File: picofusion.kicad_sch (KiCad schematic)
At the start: 33 parts, among them J1 NORTH, J2 EAST, J3 WEST, J4 SOUTH, U1 W25Q16, U2 RP2040, Y1 12MHz

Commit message: draft: schematic and layout for H20R1
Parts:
- removed C13, C15, C24, C26: 0.1uF, Capacitor_SMD:C_0201_0603Metric, symbol Device:C
- removed C25: 1uF, Capacitor_SMD:C_0201_0603Metric, symbol Device:C
- removed R2, R3: 27, Resistor_SMD:R_0201_0603Metric, symbol Device:R
- removed R4, R5: 10K, Resistor_SMD:R_0402_1005Metric, symbol Device:R
- removed U1: W25Q16, USON:8-USON, symbol Memory_Flash:W25Q32JVSS
- removed U2: RP2040, RP2040_minimal:RP2040-QFN-56, symbol MCU_RaspberryPi_RP2040:RP2040
- added U1: STM32F412CGUx, Package_DFN_QFN:QFN-48-1EP_7x7mm_P0.5mm_EP5.6x5.6mm, symbol MCU_ST_STM32F4:STM32F412CGUx
- C1: value 0.1uF -> 2u2
- C10: value 0.1uF -> 1u0
- C2, C4, C7, C9: value 0.1uF -> 0u1
- C3: value 1uF -> 0u1
- C6: value 0.1uF -> 4u7
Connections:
- net +3V3: now also C2.1, C3.1, U1.1 (VBAT), U1.24 (VDD), U1.36 (VDD), U1.48 (VDD), U1.9 (VDDA)
- net 3V3_SENSE: now also U1.15 (PA5)
- net 5V_SENSE: now also U1.14 (PA4)
- net BOOTSEL: now also U1.44 (BOOT0)
- net BUZZER: now also U1.18 (PB0)
- net CAN_SILENT: now also U1.3 (PC14)
- net DRDY_ICM42605: now also U1.30 (PA9)
- net GND: now also C1.1, U1.23 (VSS), U1.35 (VSS), U1.47 (VSS), U1.49 (VSS), U1.8 (VSSA); no longer C1.2
- net IMU_HEATER: now also U1.4 (PC15)
- net NEOPIXEL_3V3: now also U1.39 (PB3)
- net RESV1: now also U1.19 (PB1)
- net SPI0_PICO: now also U1.28 (PB15)
- net SPI0_POCI: now also U1.27 (PB14)
- net SPI0_SCK: now also U1.26 (PB13)
- net SPI0_nCS: now also U1.25 (PB12)
- net SWCLK: now also U1.37 (PA14)
- net SWDIO: now also U1.34 (PA13)
- net UART1_RX_GNSS: now also U1.38 (PA15)
- net UART1_TX_GNSS: now also U1.31 (PA10)
- net USB_DN: now also U1.32 (PA11)
- net USB_DP: now also U1.33 (PA12)
- net XIN: now also U1.5 (PH0)
- net XOUT: now also U1.6 (PH1)
- removed net +1V1: C1.1, C2.1, C3.1
- net I2C0_SCL renamed I2C1_SCL
- net I2C1_SCL: now also U1.42 (PB6)
- net I2C0_SDA renamed I2C1_SDA
- net I2C1_SDA: now also U1.43 (PB7)
- net RUN renamed nRST
- net nRST: now also U1.7 (NRST)
- net SD_nCD renamed SDIO_D0
- net SDIO_D0: now also U1.40 (PB4)
- net SPI1_PICO_SD renamed SDIO_D2
- net SDIO_D2: now also U1.17 (PA7)
- net SPI1_POCI_SD renamed SDIO_D3
- net SDIO_D3: now also U1.41 (PB5)
- net SPI1_SCK_SD renamed SDIO_CMD
- net SDIO_CMD: now also U1.16 (PA6)
- net SPI1_nCS_SD renamed SDIO_D1
- net SDIO_D1: now also U1.29 (PA8)
- net UART0_CTS_TELEM renamed UART2_CTS_TELEM
- net UART2_CTS_TELEM: now also U1.10 (PA0)
- net UART0_RTS_TELEM renamed UART2_RTS_TELEM
- net UART2_RTS_TELEM: now also U1.11 (PA1)
- net UART0_RX_TELEM renamed UART2_RX_TELEM
- net UART2_RX_TELEM: now also U1.13 (PA3)
- net UART0_TX_TELEM renamed UART2_TX_TELEM
- net UART2_TX_TELEM: now also U1.12 (PA2)
- new net: C1.2, U1.22 (VCAP_1)
- new net CAN1_RX: U1.45 (PB8)
- new net CAN1_TX: U1.46 (PB9)
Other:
- note added: "8MHz Crystal"
- note removed: "12MHz Crystal"
- note removed: "Flash"

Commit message: h20r1: more updates
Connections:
- net CAN_SILENT: now also U1.2 (PC13); no longer U1.3 (PC14)
- net IMU_HEATER: now also U1.3 (PC14); no longer U1.4 (PC15)
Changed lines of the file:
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@@
   (no_connect (at 265.43 24.13))
   (no_connect (at 69.85 88.9))
-  (no_connect (at 69.85 73.66))
+  (no_connect (at 69.85 78.74))
   (no_connect (at 265.43 21.59))
   (wire (pts (xy 54.61 60.96) (xy 49.53 60.96))
@@
     (stroke (width 0) (type default) (color 0 0 0 0))
   )
-  (wire (pts (xy 52.07 78.74) (xy 69.85 78.74))
+  (wire (pts (xy 52.07 73.66) (xy 69.85 73.66))
     (stroke (width 0) (type default) (color 0 0 0 0))
   )
@@
     (effects (font (size 1.27 1.27)) (justify left bottom))
   )
-  (label "IMU_HEATER" (at 52.07 78.74 0)
+  (label "IMU_HEATER" (at 52.07 76.2 0)
     (effects (font (size 1.27 1.27)) (justify left bottom))
   )
@@
     (effects (font (size 1.27 1.27)) (justify left bottom))
   )
-  (label "CAN_SILENT" (at 52.07 76.2 0)
-    (effects (font (size 1.27 1.27)) (justify left bottom))
-  )
+  (label "CAN_SILENT" (at 52.07 73.66 0)
+    (effects (font (size 1.27 1.27)) (justify left bottom))
+  )

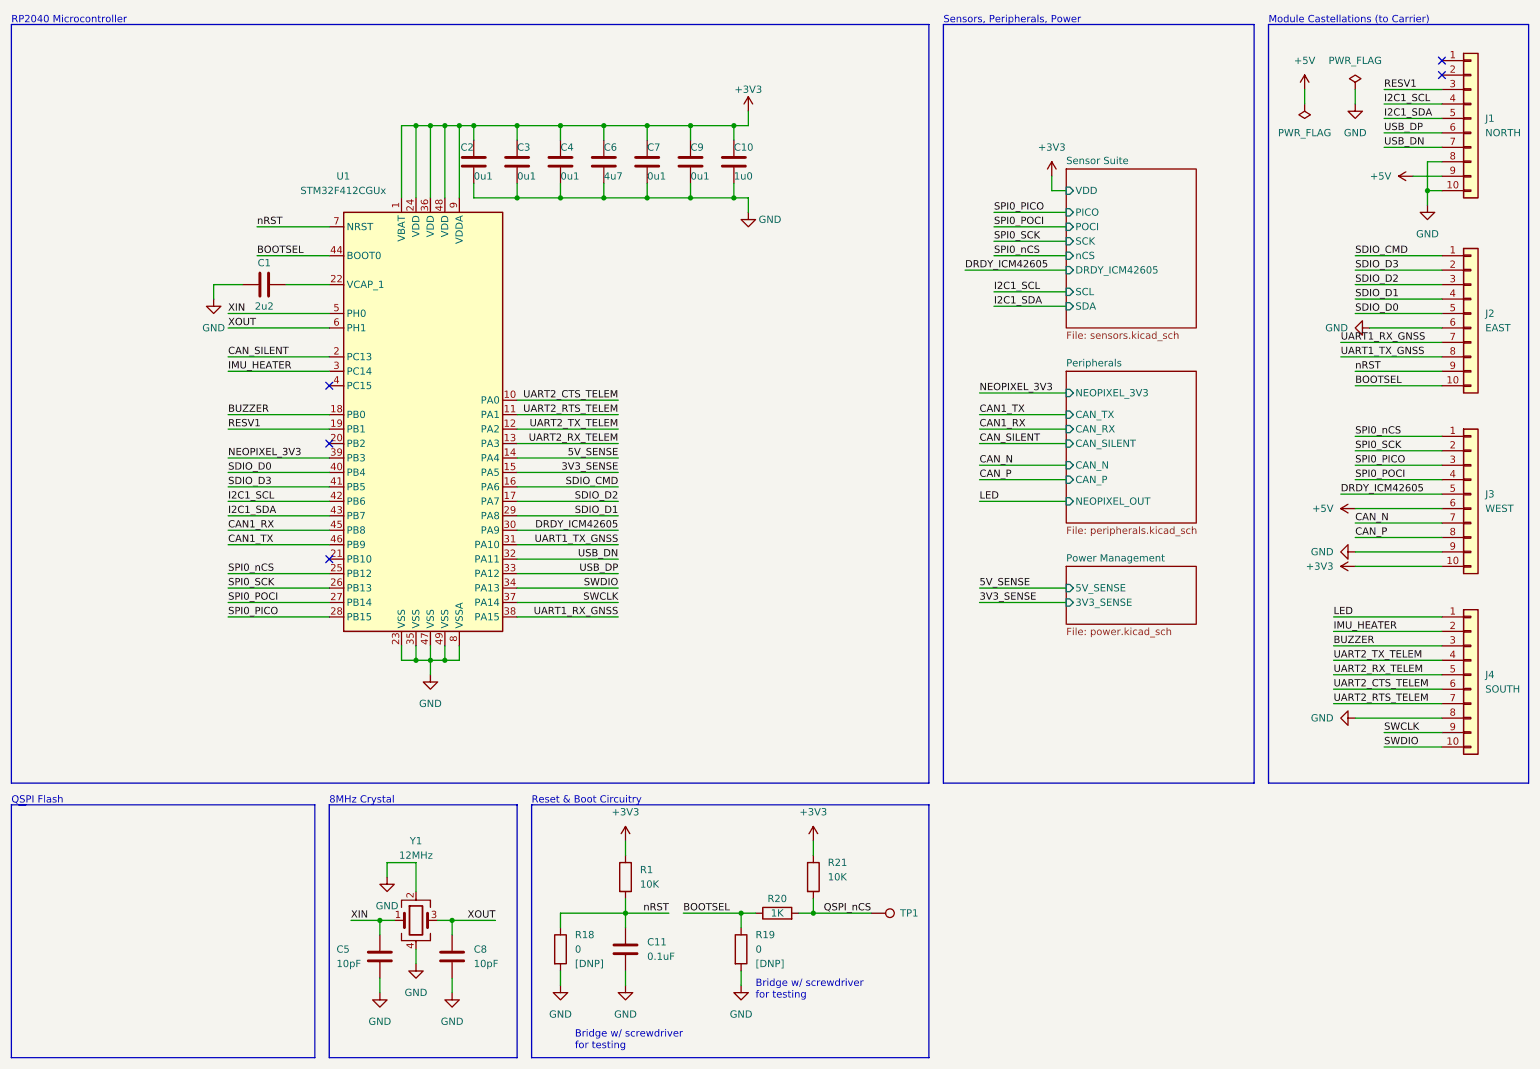
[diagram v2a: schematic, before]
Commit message: replace sdio with spi2, finish routing, front silkscreen
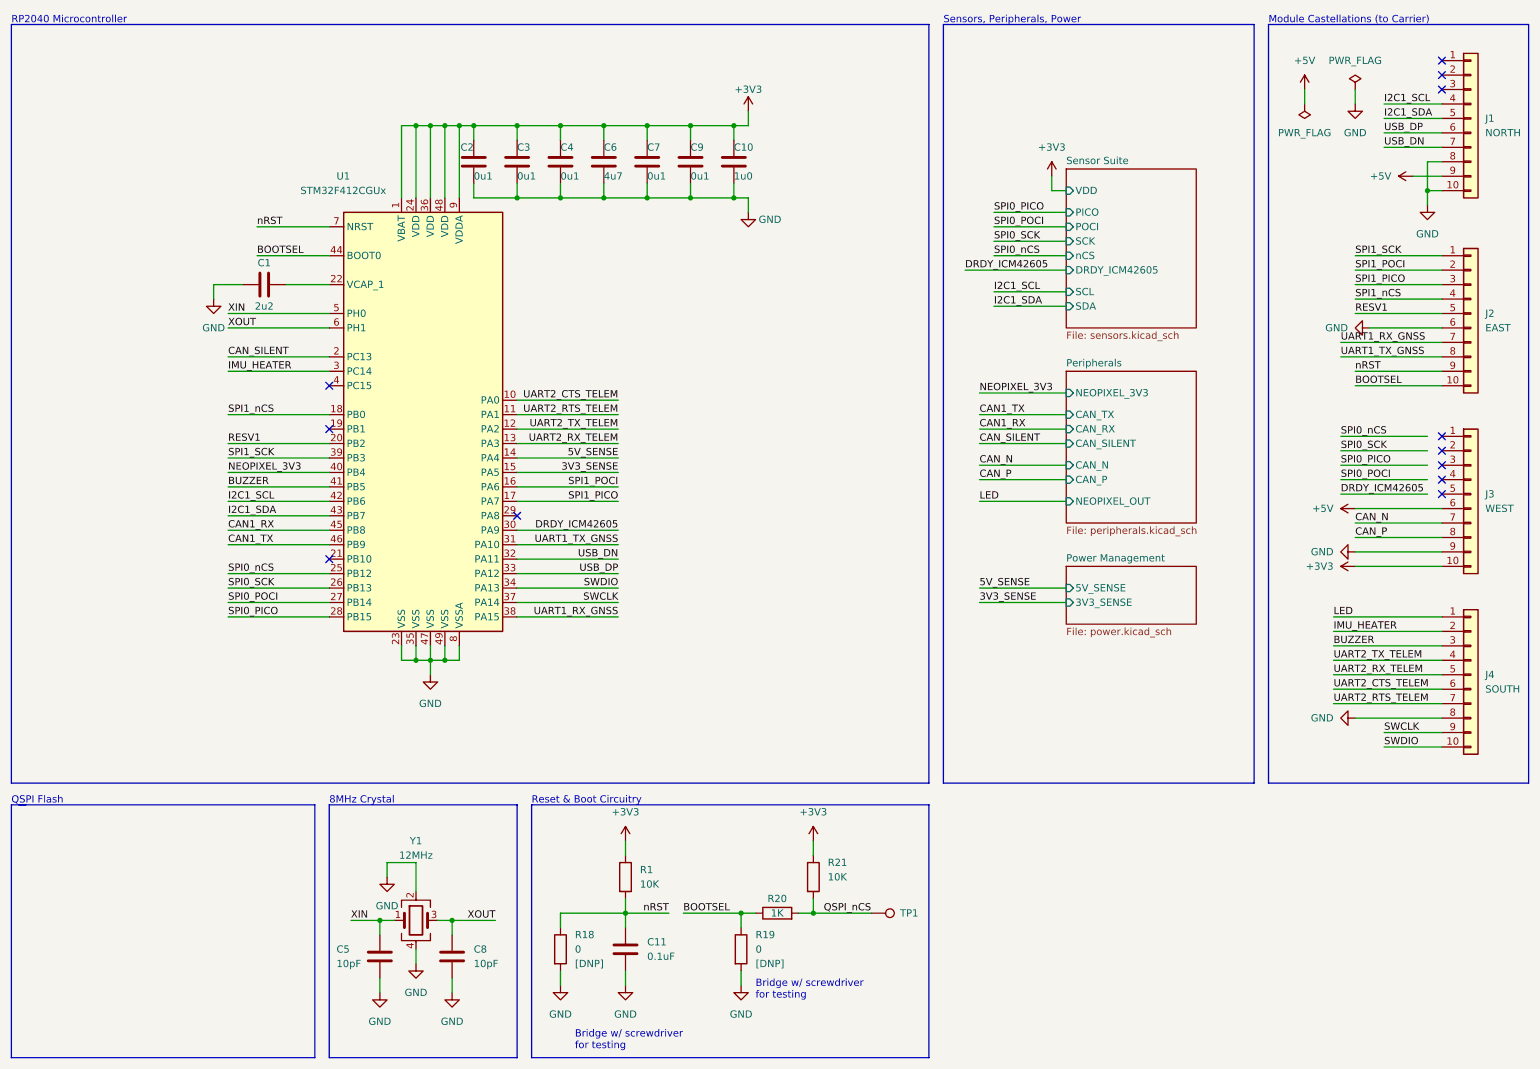
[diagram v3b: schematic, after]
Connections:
- net BUZZER: now also U1.41 (PB5); no longer U1.18 (PB0)
- net DRDY_ICM42605: no longer J3.5 (Pin_5)
- net NEOPIXEL_3V3: now also U1.40 (PB4); no longer U1.39 (PB3)
- net RESV1: now also J2.5 (Pin_5), U1.20 (PB2); no longer J1.3 (Pin_3), U1.19 (PB1)
- net SPI0_PICO: no longer J3.3 (Pin_3)
- net SPI0_POCI: no longer J3.4 (Pin_4)
- net SPI0_SCK: no longer J3.2 (Pin_2)
- net SPI0_nCS: no longer J3.1 (Pin_1)
- net SDIO_CMD renamed SPI1_POCI
- net SPI1_POCI: now also J2.2 (Pin_2); no longer J2.1 (Pin_1)
- removed net SDIO_D0: J2.5 (Pin_5), U1.40 (PB4)
- net SDIO_D1: no longer names the net of U1.29 (PA8)
- net SDIO_D1: no longer J2.4 (Pin_4)
- net SDIO_D2 renamed SPI1_PICO
- removed net SDIO_D3: J2.2 (Pin_2), U1.41 (PB5)
- new net SPI1_SCK: J2.1 (Pin_1), U1.39 (PB3)
- new net SPI1_nCS: J2.4 (Pin_4), U1.18 (PB0)
- no-connect marks 5 -> 12

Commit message: cleanup and review of PicoFusion H20 R1
* update to KiCad 7
* add thermal vias to STM32F412CG QFN footprint
* update silkscreen branding
* update applicable silkscreen to Kicad 7 native text
* fix UART GNSS TX/RX swapped
* minor routing changes and cleanup
* replace DNP jump resistors with unpopulated test point footprint
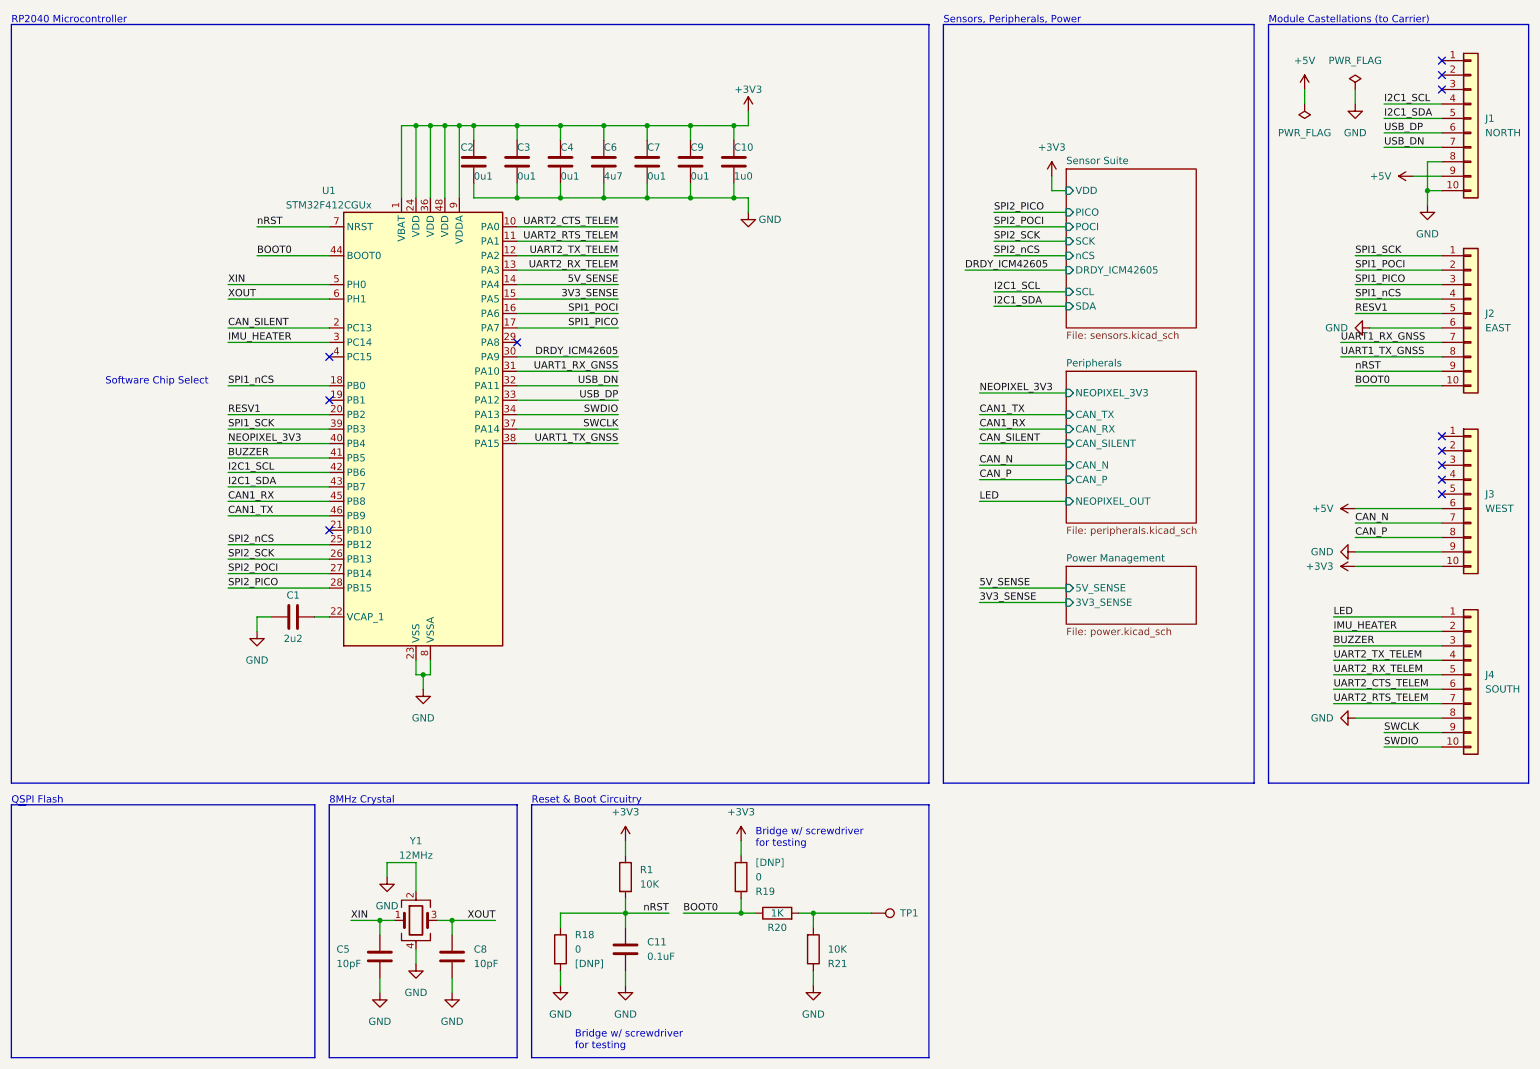
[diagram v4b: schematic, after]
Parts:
- R18, R19: footprint Resistor_SMD:R_0402_1005Metric -> TestPoint_Extra:TestPoint_2Pin_0402_1005Metric
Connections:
- net +3V3: now also R19.2; no longer R21.1
- net GND: now also R21.1; no longer R19.2
- net UART1_RX_GNSS: now also U1.31 (PA10); no longer U1.38 (PA15)
- net UART1_TX_GNSS: now also U1.38 (PA15); no longer U1.31 (PA10)
- net BOOTSEL renamed BOOT0
- net QSPI_nCS: no longer names the net of R20.2, R21.2, TP1.1
- net SPI0_PICO renamed SPI2_PICO
- net SPI0_POCI renamed SPI2_POCI
- net SPI0_SCK renamed SPI2_SCK
- net SPI0_nCS renamed SPI2_nCS
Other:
- note added: "Software Chip Select"
- moved on the sheet: C1, R19, R21

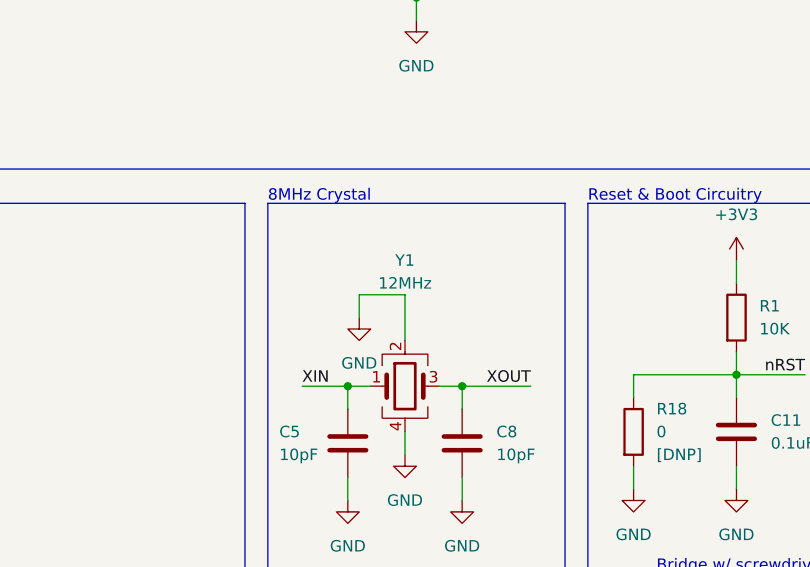
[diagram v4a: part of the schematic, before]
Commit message: update crystal
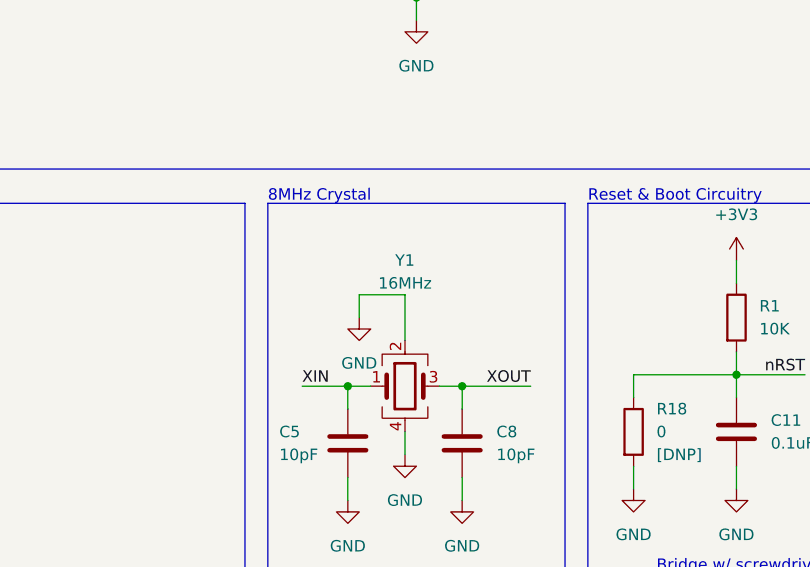
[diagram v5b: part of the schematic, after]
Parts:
- Y1: value 12MHz -> 16MHz; footprint Crystal:Crystal_SMD_2520-4Pin_2.5x2.0mm -> Crystal:Crystal_SMD_2016-4Pin_2.0x1.6mm
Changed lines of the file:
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@@
       (effects (font (size 1.27 1.27)))
     )
-    (property "Value" "12MHz" (at 85.09 161.29 0)
+    (property "Value" "16MHz" (at 85.09 161.29 0)
       (effects (font (size 1.27 1.27)))
     )
-    (property "Footprint" "Crystal:Crystal_SMD_2520-4Pin_2.5x2.0mm" (at 85.09 172.72 0)
+    (property "Footprint" "Crystal:Crystal_SMD_2016-4Pin_2.0x1.6mm" (at 85.09 172.72 0)
       (effects (font (size 1.27 1.27)) hide)
     )
